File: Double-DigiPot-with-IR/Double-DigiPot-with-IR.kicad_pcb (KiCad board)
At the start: 2 copper layers, 37.6 x 58.2 mm, 24 parts, among them J1 Conn_01x09_Pin, SW1 SW_Push_DPDT, SW2 EVQ-P7A01P, SW3 EVQ-P7A01P, U1 ATtiny404-SS, U2 MCP4561T-103E/MS, U3 MCP4561T-103E/MS, U4 TSOP382xx, U5 AMS1117-3.3

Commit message: MEGA UPDATE (Redesign) (It might work now)
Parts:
- removed SW2, SW3: EVQ-P7A01P, EdgeSwitch:EVQ_P7_PAN
- removed U5: AMS1117-3.3, Package_TO_SOT_SMD:SOT-223-3_TabPin2
- added C10: 100n, Capacitor_SMD:C_0805_2012Metric_Pad1.18x1.45mm_HandSolder, F.Cu at (190.6, 82.0)
- added C7: 100n, Capacitor_SMD:C_0805_2012Metric_Pad1.18x1.45mm_HandSolder, F.Cu at (188.0, 82.0)
- added C8: 100n, Capacitor_SMD:C_0805_2012Metric_Pad1.18x1.45mm_HandSolder, F.Cu at (193.0, 82.0)
- added C9: 100n, Capacitor_SMD:C_0805_2012Metric_Pad1.18x1.45mm_HandSolder, F.Cu at (183.5, 82.0)
- added R10: 10k, Resistor_SMD:R_0805_2012Metric_Pad1.20x1.40mm_HandSolder, F.Cu at (192.6, 90.4)
- added R11: 10k, Resistor_SMD:R_0805_2012Metric_Pad1.20x1.40mm_HandSolder, F.Cu at (192.6, 87.2)
- added R12: 4.7k, Resistor_SMD:R_0805_2012Metric_Pad1.20x1.40mm_HandSolder, F.Cu at (197.4, 98.4)
- added R13: 4.7k, Resistor_SMD:R_0805_2012Metric_Pad1.20x1.40mm_HandSolder, F.Cu at (200.2, 100.5)
- added R8: 10k, Resistor_SMD:R_0805_2012Metric_Pad1.20x1.40mm_HandSolder, F.Cu at (187.8, 87.2)
- added R9: 10k, Resistor_SMD:R_0805_2012Metric_Pad1.20x1.40mm_HandSolder, F.Cu at (187.8, 90.4)
- added TP3: GNDPoint, TestPoint:TestPoint_Pad_D4.0mm, F.Cu at (207.5, 94.5)
- added U6: MC78L05_SOT89, Package_TO_SOT_SMD:SOT-89-3_Handsoldering, F.Cu at (198.5, 83.5)
- C1, C2, C3, C4: footprint Capacitor_SMD:C_0805_2012Metric -> Capacitor_SMD:C_0805_2012Metric_Pad1.18x1.45mm_HandSolder
- C5, C6: value 47u -> 10u; footprint Capacitor_SMD:C_1210_3225Metric -> Capacitor_SMD:C_0805_2012Metric_Pad1.18x1.45mm_HandSolder
- R1, R6: value 4.7k -> 330; footprint Resistor_SMD:R_0805_2012Metric -> Resistor_SMD:R_0805_2012Metric_Pad1.20x1.40mm_HandSolder
- R2: value 4.7k -> 330; footprint Capacitor_SMD:C_0805_2012Metric -> Resistor_SMD:R_0805_2012Metric_Pad1.20x1.40mm_HandSolder
- R3, R5: footprint Resistor_SMD:R_0805_2012Metric -> Resistor_SMD:R_0805_2012Metric_Pad1.20x1.40mm_HandSolder
- R4: footprint Capacitor_SMD:C_0805_2012Metric -> Resistor_SMD:R_0805_2012Metric_Pad1.20x1.40mm_HandSolder
- SW1: footprint DigiPot:CONN_S2273_APM -> digiPot:CONN_S2273_APM
- U2, U3: footprint DigiPot:MSOP8_MC_MCH -> digiPot:MSOP8_MC_MCH
- moved R2 24.5 mm to (185.8, 127.0)
- moved C1 22.8 mm to (185.8, 121.6), turned to 90 degrees
- moved U1 18.0 mm to (192.0, 121.0), turned to 90 degrees
- moved R4 17.2 mm to (198.5, 108.1), turned to 180 degrees
- moved C2 15.9 mm to (177.0, 100.5)
- moved C3 14.7 mm to (187.5, 100.5)
- moved R3 13.5 mm to (194.2, 103.3), turned to 90 degrees
- moved U2 11.8 mm to (180.0, 101.5)
- moved U3 11.5 mm to (190.5, 101.5)
- moved R1 11.3 mm to (185.8, 116.2)
- moved C5 6.85 mm to (197.0, 90.0), turned to -90 degrees
- moved TP1 4.95 mm to (207.5, 108.5)
- moved TP2 4.95 mm to (207.5, 101.5)
- moved R5 4.54 mm to (203.0, 102.6)
- moved C6 2.55 mm to (200.0, 90.0), turned to -90 degrees
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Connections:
- net 3.3 renamed 5
- J1 pad 4: Rin -> Net-(J1-Pin_4)
- J1 pad 5: Lin -> Net-(J1-Pin_5)
- J1 pad 7: Rout -> Net-(J1-Pin_7)
- J1 pad 8: Lout -> Net-(J1-Pin_8)
- R1 pad 2: Net-(U1-PA7) -> Net-(U1-PA3)
- R2 pad 1: Net-(U1-PA6) -> Net-(U1-PA5)
- R6 pad 1: Net-(U1-PA1) -> Net-(U1-PA4)
- SW1 pad 5: Net-(U1-PA1) -> Net-(U1-PA7)
- U1 pad 11: Net-(U1-PA1) -> unconnected-(U1-PA1-Pad11)
- U1 pad 13: unconnected-(U1-PA3-Pad13) -> Net-(U1-PA3)
- U1 pad 4: Net-(U1-PA6) -> unconnected-(U1-PA6-Pad4)
- U2 pad 7: GND -> /ref
- U3 pad 7: GND -> /ref
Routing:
- net Net-(U1-PA1): track 45.6 -> 0.00 mm, vias 2 -> 0
- net /ref: track 0.00 -> 23.3 mm, vias 0 -> 2
- net Net-(U1-PB3): track 29.6 -> 9.97 mm
- net 5: track 19.1 -> 2.20 mm, vias 4 -> 0
- net Net-(U1-~{RESET}/PA0): track 4.09 -> 19.0 mm, vias 0 -> 2
- net GND: track 24.9 -> 12.0 mm, vias 11 -> 53
- net Net-(U1-PA5): track 18.5 -> 5.96 mm
- net Net-(J1-Pin_7): track 0.00 -> 11.9 mm
- net Net-(U1-PA4): track 19.3 -> 7.93 mm
- net TXD: track 13.5 -> 24.5 mm
- net Net-(D1-BA): track 13.7 -> 3.10 mm
- net Net-(U1-PA7): track 4.71 -> 13.4 mm
- net Lout: track 11.1 -> 17.7 mm, vias 0 -> 2
- net Net-(U1-PB1): track 28.4 -> 34.8 mm, vias 4 -> 2
- net Net-(U1-PB0): track 28.9 -> 35.2 mm, vias 0 -> 2
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- added copper zone on F.Cu, net GND
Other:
- board text added: "A"

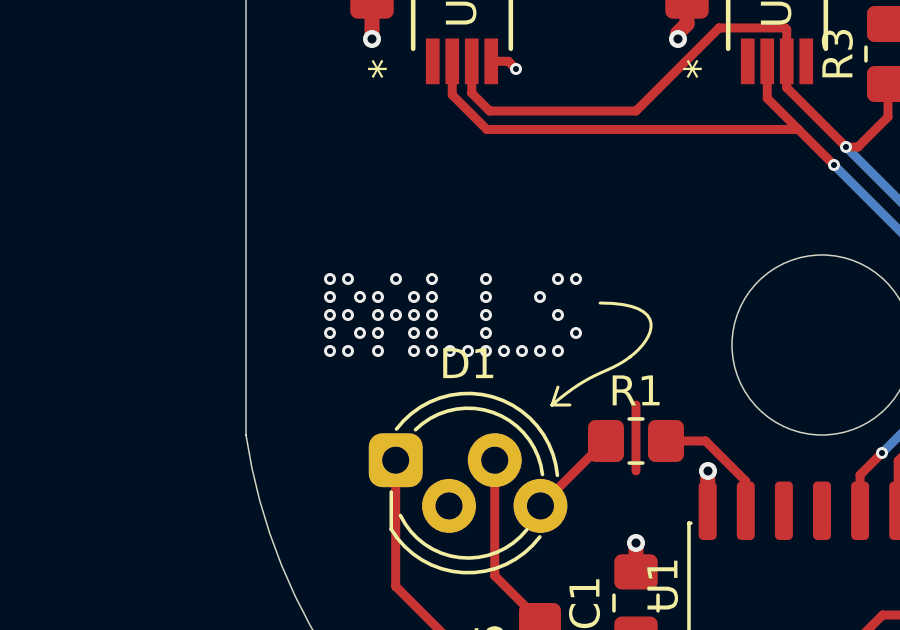
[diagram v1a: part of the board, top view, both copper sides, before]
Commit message: Update PCB so we can verify that everything got updated
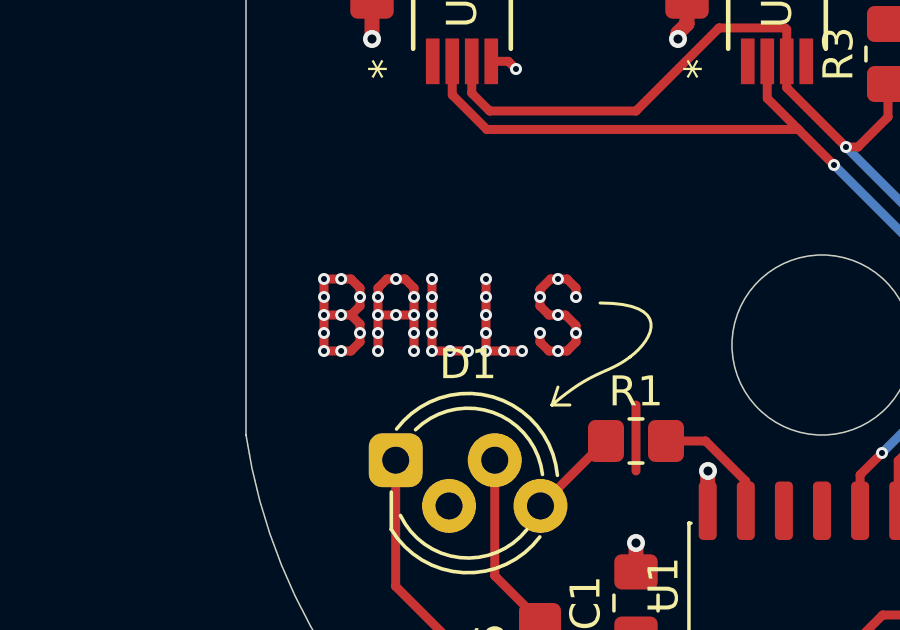
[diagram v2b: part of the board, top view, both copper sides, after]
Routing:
- net GND: track 12.0 -> 40.1 mm
